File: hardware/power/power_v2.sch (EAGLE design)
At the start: 43 parts, among them J1 FASTON1289_ST, J2 FASTON1289_ST, J3 12v, J4 5v, J5 XT30PW-F, J6 XT30PW-F, J7 XT30PW-F, J8 XT30PW-F, Q1 MMBT5401L, Q2 PSMN1R0-40YSH, U1 PDQ30-Q24-S5-D, U2 PDQ30-Q24-S12-D

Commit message: Going to rework power plane v2
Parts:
- added C11: 0.01uF, timlib:C_CERAMIC_1210
- added C12: 2.2n, timlib:C_CERAMIC_1210
- added C13: 16nF, timlib:C_CERAMIC_1210
- added D3: SMAJ30A, timlib:SMAJ30A
- added D4: SK510A-LTP, timlib:SK510A-LTP
- added Q3: MMBT5401L, timlib:MMBT5401L
- added Q4: PSMN1R0-40YSH, timlib:PSMN1R0-40YSH
- added R10: 18.9k, rcl:R-US_R0603
- added R11: 18.9, rcl:R-US_R0603
- added R12: PMR25HZPFV, timlib:PMR25HZPFV
- added R7: 47.5k, rcl:R-US_R0603
- added R8: 3.4k, rcl:R-US_R0603
- added R9: 4.32k, rcl:R-US_R0603
- added U$13: 2-PIN, timlib:2-PIN
- added U$14: LM5069_DGS_10, timlib:LM5069_DGS_10
- added U$22: 1N4148W-7-F, timlib:1N4148W-7-F
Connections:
- removed net ISO_GND: U1.-VIN, U2.-VIN
- new net MOSFET_DRAIN1: Q4.D, R12.2
- new net N$12: R8.2, R9.1, U$14.OVLO
- new net N$13: R7.1, U$13.P$2
- new net N$14: Q4.G, R11.1, U$14.GATE, U$22.A
- new net N$15: R10.1, U$14.PWR
- new net N$16: C12.1, U$14.TIMER
- new net N$17: C13.1, Q3.E, U$22.C
- new net N$18: Q3.B, R11.2
- new net N$19: R12.1K, U$14.VIN
- new net N$20: R12.2K, U$14.SEN
- new net N$4: R7.2, R8.1, U$14.UVLO
- net +24V_BATT: now also C11.1, D3.C, R12.1, U$13.P$1; no longer U1.+VIN, U2.+VIN
- net +24V_ISO: now also D4.C, Q4.S, U$14.OUT, U1.+VIN, U2.+VIN
- net GND_BATT: now also C11.2, C12.2, C13.2, D3.A, D4.A, Q3.C, R10.2, R9.2, U$14.GND, U1.-VIN, U2.-VIN

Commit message: Happy with this layout
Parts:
- removed C11: 0.01uF, timlib:C_CERAMIC_1210
- removed U$6: 1N4148W-7-F, timlib:1N4148W-7-F
- D3: value SMAJ30A -> 1N4148W-7-F; device timlib:SMAJ30A -> timlib:1N4148W-7-F
- renumbered U$22 to D5
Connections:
- net +24V_BATT: no longer C11.1, D3.C
- net GND_BATT: no longer C11.2, D3.A
- net N$5: now also D3.A; no longer U$6.A
- net N$8: now also D3.C; no longer U$6.C

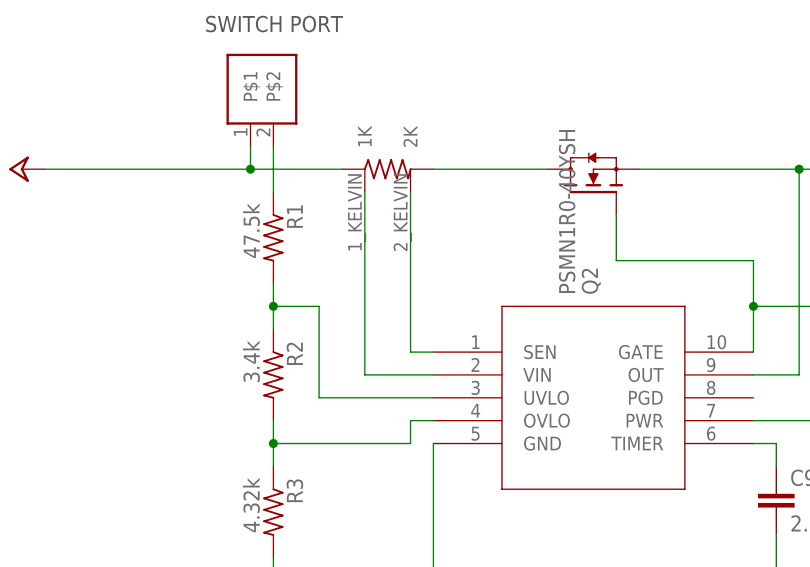
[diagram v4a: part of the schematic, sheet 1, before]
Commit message: Added more accurate current limit resistors
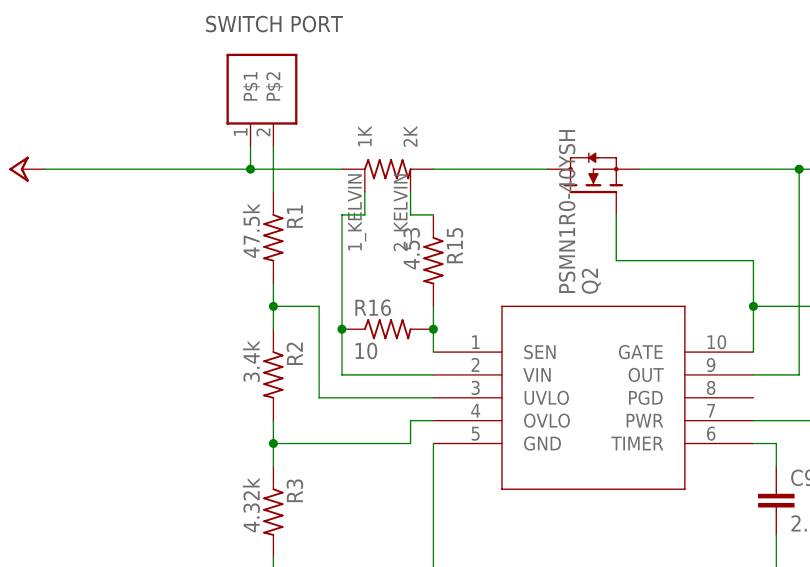
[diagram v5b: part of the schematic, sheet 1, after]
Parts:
- added R13, R16: 10, rcl:R-US_R0603
- added R14, R15: 4.53, rcl:R-US_R0603
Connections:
- new net N$21: R12.2K, R14.1
- new net N$22: R12.1K, R13.2, U$14.VIN
- net N$10: now also R15.2, R16.2, U$1.SEN; no longer R4.1K, U$1.VIN
- net N$11: now also R15.1; no longer U$1.SEN
- net N$19: now also R16.1, R4.1K, U$1.VIN; no longer R12.1K, U$14.VIN
- net N$20: now also R13.1, R14.2; no longer R12.2K
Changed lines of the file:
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@@
 <part name="D3" library="timlib" library_urn="urn:adsk.eagle:library:16152524" deviceset="1N4148W-7-F" device="" package3d_urn="urn:adsk.eagle:package:16502213/2"/>
 <part name="D5" library="timlib" library_urn="urn:adsk.eagle:library:16152524" deviceset="1N4148W-7-F" device="" package3d_urn="urn:adsk.eagle:package:16502213/2"/>
+<part name="R13" library="rcl" library_urn="urn:adsk.eagle:library:334" deviceset="R-US_" device="R0603" package3d_urn="urn:adsk.eagle:package:23555/3" value="10"/>
+<part name="R14" library="rcl" library_urn="urn:adsk.eagle:library:334" deviceset="R-US_" device="R0603" package3d_urn="urn:adsk.eagle:package:23555/3" value="4.53"/>
+<part name="R15" library="rcl" library_urn="urn:adsk.eagle:library:334" deviceset="R-US_" device="R0603" package3d_urn="urn:adsk.eagle:package:23555/3" value="4.53"/>
+<part name="R16" library="rcl" library_urn="urn:adsk.eagle:library:334" deviceset="R-US_" device="R0603" package3d_urn="urn:adsk.eagle:package:23555/3" value="10"/>
 </parts>
 <sheets>
@@
 <attribute name="NAME" x="180.34" y="106.68" size="1.778" layer="95"/>
 <attribute name="VALUE" x="180.34" y="100.33" size="1.778" layer="96"/>
+</instance>
+<instance part="R15" gate="G$1" x="119.38" y="114.3" smashed="yes" rot="R270">
+<attribute name="NAME" x="120.8786" y="118.11" size="1.778" layer="95" rot="R270"/>
+<attribute name="VALUE" x="116.078" y="118.11" size="1.778" layer="96" rot="R270"/>
+</instance>
+<instance part="R16" gate="G$1" x="114.3" y="106.68" smashed="yes">
+<attribute name="NAME" x="110.49" y="108.1786" size="1.778" layer="95"/>
+<attribute name="VALUE" x="110.49" y="103.378" size="1.778" layer="96"/>
 </instance>
 </instances>
@@
 <net name="N$10" class="0">
 <segment>
+<pinref part="U$1" gate="A" pin="SEN"/>
+<pinref part="R16" gate="G$1" pin="2"/>
+<wire x1="119.38" y1="104.14" x2="119.38" y2="106.68" width="0.1524" layer="91"/>
+<pinref part="R15" gate="G$1" pin="2"/>
+<wire x1="119.38" y1="106.68" x2="119.38" y2="109.22" width="0.1524" layer="91"/>
+<junction x="119.38" y="106.68"/>
+</segment>
+</net>
+<net name="N$11" class="0">
+<segment>
+<pinref part="R15" gate="G$1" pin="1"/>
+<pinref part="R4" gate="A" pin="2K"/>
+<wire x1="119.38" y1="119.38" x2="116.84" y2="119.38" width="0.1524" layer="91"/>
+<wire x1="116.84" y1="119.38" x2="116.84" y2="121.92" width="0.1524" layer="91"/>
+</segment>
+</net>
+<net name="N$19" class="0">
+<segment>
+<pinref part="R4" gate="A" pin="1K"/>
+<wire x1="111.76" y1="121.92" x2="111.76" y2="119.38" width="0.1524" layer="91"/>
+<wire x1="111.76" y1="119.38" x2="109.22" y2="119.38" width="0.1524" layer="91"/>
+<pinref part="R16" gate="G$1" pin="1"/>
+<wire x1="109.22" y1="119.38" x2="109.22" y2="106.68" width="0.1524" layer="91"/>
 <pinref part="U$1" gate="A" pin="VIN"/>
-<wire x1="119.38" y1="101.6" x2="111.76" y2="101.6" width="0.1524" layer="91" grouprefs="LEG_SOFTSTART"/>
-<pinref part="R4" gate="A" pin="1K"/>
-<wire x1="111.76" y1="121.92" x2="111.76" y2="101.6" width="0.1524" layer="91" grouprefs="LEG_SOFTSTART"/>
-</segment>
-</net>
-<net name="N$11" class="0">
-<segment>
-<pinref part="R4" gate="A" pin="2K"/>
-<wire x1="116.84" y1="121.92" x2="116.84" y2="104.14" width="0.1524" layer="91" grouprefs="LEG_SOFTSTART"/>
-<pinref part="U$1" gate="A" pin="SEN"/>
-<wire x1="116.84" y1="104.14" x2="119.38" y2="104.14" width="0.1524" layer="91" grouprefs="LEG_SOFTSTART"/>
+<wire x1="109.22" y1="106.68" x2="109.22" y2="101.6" width="0.1524" layer="91"/>
+<wire x1="109.22" y1="101.6" x2="119.38" y2="101.6" width="0.1524" layer="91"/>
+<junction x="109.22" y="106.68"/>
 </segment>
 </net>
@@
 <attribute name="NAME" x="142.24" y="96.52" size="1.778" layer="95"/>
 <attribute name="VALUE" x="142.24" y="90.17" size="1.778" layer="96"/>
+</instance>
+<instance part="R13" gate="G$1" x="76.2" y="96.52" smashed="yes" rot="R180">
+<attribute name="NAME" x="80.01" y="95.0214" size="1.778" layer="95" rot="R180"/>
+<attribute name="VALUE" x="80.01" y="99.822" size="1.778" layer="96" rot="R180"/>
+</instance>
+<instance part="R14" gate="G$1" x="81.28" y="104.14" smashed="yes" rot="R270">
+<attribute name="NAME" x="82.7786" y="107.95" size="1.778" layer="95" rot="R270"/>
+<attribute name="VALUE" x="77.978" y="107.95" size="1.778" layer="96" rot="R270"/>
 </instance>
 </instances>
@@
 </segment>
 </net>
-<net name="N$19" class="0">
-<segment>
-<wire x1="81.28" y1="91.44" x2="73.66" y2="91.44" width="0.1524" layer="91" grouprefs="ISO_SOFTSTART"/>
-<wire x1="73.66" y1="111.76" x2="73.66" y2="91.44" width="0.1524" layer="91" grouprefs="ISO_SOFTSTART"/>
+<net name="N$20" class="0">
+<segment>
+<wire x1="81.28" y1="96.52" x2="81.28" y2="93.98" width="0.1524" layer="91" grouprefs="ISO_SOFTSTART"/>
+<pinref part="U$14" gate="A" pin="SEN"/>
+<pinref part="R13" gate="G$1" pin="1"/>
+<pinref part="R14" gate="G$1" pin="2"/>
+<wire x1="81.28" y1="96.52" x2="81.28" y2="99.06" width="0.1524" layer="91"/>
+<junction x="81.28" y="96.52"/>
+</segment>
+</net>
+<net name="N$21" class="0">
+<segment>
+<pinref part="R14" gate="G$1" pin="1"/>
+<pinref part="R12" gate="A" pin="2K"/>
+<wire x1="81.28" y1="109.22" x2="78.74" y2="109.22" width="0.1524" layer="91"/>
+<wire x1="78.74" y1="109.22" x2="78.74" y2="111.76" width="0.1524" layer="91"/>
+</segment>
+</net>
+<net name="N$22" class="0">
+<segment>
+<pinref part="R12" gate="A" pin="1K"/>
+<wire x1="73.66" y1="111.76" x2="73.66" y2="109.22" width="0.1524" layer="91"/>
+<wire x1="73.66" y1="109.22" x2="71.12" y2="109.22" width="0.1524" layer="91"/>
+<pinref part="R13" gate="G$1" pin="2"/>
+<wire x1="71.12" y1="109.22" x2="71.12" y2="96.52" width="0.1524" layer="91"/>
+<wire x1="81.28" y1="91.44" x2="71.12" y2="91.44" width="0.1524" layer="91" grouprefs="ISO_SOFTSTART"/>
 <pinref part="U$14" gate="A" pin="VIN"/>
-<pinref part="R12" gate="A" pin="1K"/>
-</segment>
-</net>
-<net name="N$20" class="0">
-<segment>
-<wire x1="78.74" y1="111.76" x2="78.74" y2="93.98" width="0.1524" layer="91" grouprefs="ISO_SOFTSTART"/>
-<wire x1="78.74" y1="93.98" x2="81.28" y2="93.98" width="0.1524" layer="91" grouprefs="ISO_SOFTSTART"/>
-<pinref part="U$14" gate="A" pin="SEN"/>
-<pinref part="R12" gate="A" pin="2K"/>
-</segment>
-</net>
+<wire x1="71.12" y1="96.52" x2="71.12" y2="91.44" width="0.1524" layer="91"/>
+<junction x="71.12" y="96.52"/>
+</segment>
+</net>

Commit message: Reordered schematic
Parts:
- R12, R4: value PMR25HZPFV -> PMR25HZPFV1L00; device timlib:PMR25HZPFV -> timlib:PMR25HZPFV1L00
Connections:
- net +24V_LEG renamed +24V_POWER
- net MOSFET_DRAIN: now also R12.2; no longer R4.2
- net MOSFET_DRAIN1: now also R4.2; no longer R12.2
- net N$11: now also R12.2K; no longer R4.2K
- net N$19: now also R12.1K; no longer R4.1K
- net N$21: now also R4.2K; no longer R12.2K
- net N$22: now also R4.1K; no longer R12.1K

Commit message: Updates to power board
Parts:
- removed C23: 10uF, timlib:C_CERAMIC_1210
- removed U$13, U$26: 2-PIN, timlib:2-PIN
- added C11: 2.2nF, rcl:C-EUC0603
- added H1, H2, H3, H4, H5, H6: GND_HOLE_M3, timlib:GND_HOLE_M3
- added J100, J101: FASTON1289_ST, timlib:FASTON1289_ST
- C1, C2, C3, C4, C5, C6, C7: value 220uf -> 10uF; device timlib:35ZLH220MEFC8X11.5 -> timlib:C_CERAMIC_1210
- C10: value 16nF -> 10uF
- C12: value 2.2n -> 0.01uF
- C13: value 16nF -> 47nF; device timlib:C_CERAMIC_1210 -> rcl:C-EUC0603
- C14: value 10uF -> 2.2nF; device timlib:C_CERAMIC_1210 -> rcl:C-EUC0603
- C15, C17, C18, C19, C20, C21, C22: value 10uF -> 220uf; device timlib:C_CERAMIC_1210 -> timlib:35ZLH220MEFC8X11.5
- C16: value 10uF -> 47nF; device timlib:C_CERAMIC_1210 -> rcl:C-EUC0603
- C8: value 0.01uF -> 2.2nF
- C9: value 2.2n -> 10uF
- D1: value SMAJ30A -> SK510A-LTP; device timlib:SMAJ30A -> timlib:SK510A-LTP
- D2: value SK510A-LTP -> SMAJ30A; device timlib:SK510A-LTP -> timlib:SMAJ30A
- D4: value SK510A-LTP -> 1N4148W-7-F; device timlib:SK510A-LTP -> timlib:1N4148W-7-F
- D5: value 1N4148W-7-F -> SK510A-LTP; device timlib:1N4148W-7-F -> timlib:SK510A-LTP
- J1: value FASTON1289_ST -> 12v; device timlib:FASTON1289_ST -> timlib:MOLEX_4_RA
- J2: value FASTON1289_ST -> 5v; device timlib:FASTON1289_ST -> timlib:MOLEX_4_RA
- J3: value 12v -> XT30PW-F; device timlib:MOLEX_4_RA -> timlib:XT30PW-F
- J4: value 5v -> XT30PW-F; device timlib:MOLEX_4_RA -> timlib:XT30PW-F
- J7, J8: value XT30PW-F -> 2-PIN; device timlib:XT30PW-F -> timlib:2-PIN
- Q1: value MMBT5401L -> PSMN1R0-40YSH; device timlib:MMBT5401L -> timlib:PSMN1R0-40YSH
- Q2: value PSMN1R0-40YSH -> MMBT5401L; device timlib:PSMN1R0-40YSH -> timlib:MMBT5401L
- R1: value 47.5k -> 4.32k
- R10: value 18.9k -> 3.4k
- R11: value 18.9 -> 1k
- R12: value PMR25HZPFV1L00 -> 18.9k; device timlib:PMR25HZPFV1L00 -> rcl:R-US_R0603
- R13: value 10 -> 18.9k
- R15: value 4.53 -> 4.32k
- R16: value 10 -> 1k
- R3, R9: value 4.32k -> 47.5k
- R4: value PMR25HZPFV1L00 -> 4.53; device timlib:PMR25HZPFV1L00 -> rcl:R-US_R0603
- R5: value 18.9k -> 10
- R6: value 18.9 -> 10
- R7: value 47.5k -> 0.002; device rcl:R-US_R0603 -> timlib:PMR25HZPFV2L00
- R8: value 3.4k -> 0.002; device rcl:R-US_R0603 -> timlib:PMR25HZPFV2L00
- U1: value PDQ30-Q24-S5-D -> PDQ30-Q24-S12-D; device timlib:PDQ30-Q24-S5-D -> timlib:PDQ30-Q24-S12-D
- U2: value PDQ30-Q24-S12-D -> PDQ30-Q24-S5-D; device timlib:PDQ30-Q24-S12-D -> timlib:PDQ30-Q24-S5-D
- renumbered U$1 to U3, U$14 to U4
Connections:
- net +12VOUT: now also J1.CONN2, J1.CONN4, U1.+12VOUT; no longer J3.CONN2, J3.CONN4, U2.+12VOUT
- net +24V_BATT: now also C12.1, D2.C, J101.PIN1, J7.P$1, J8.P$1, R7.1, R8.1; no longer C8.1, D1.C, J1.PIN1, R12.1, R4.1, U$13.P$1, U$26.P$1
- net +24V_ISO: now also C1.1, C10.1, C2.1, C3.1, C4.1, C5.1, C6.1, C7.1, C8.1, C9.1, D1.C, Q1.S; no longer C14.1, C15.1, C16.1, C17.1, C18.1, C19.1, C20.1, C21.1, C22.1, C23.1, D4.C, Q4.S
- net +24V_POWER: now also C15.+, C17.+, C18.+, C19.+, C20.+, C21.+, C22.+, D5.C, J3.V+, J4.V+, Q4.S; no longer C1.+, C2.+, C3.+, C4.+, C5.+, C6.+, C7.+, D2.C, J7.V+, J8.V+, Q2.S
- net +5VOUT: now also J2.CONN2, J2.CONN4, U2.+5VOUT; no longer J4.CONN2, J4.CONN4, U1.+5VOUT
- net 12V_GND: now also J1.CONN1, J1.CONN3, U1.12V_GND; no longer J3.CONN1, J3.CONN3, U2.12V_GND
- net 5V_GND: now also J2.CONN1, J2.CONN3, U2.5V_GND; no longer J4.CONN1, J4.CONN3, U1.5V_GND
- net GND_BATT: now also C1.2, C11.2, C15.-, C17.-, C18.-, C19.-, C2.2, C20.-, C21.-, C22.-, C3.2, C4.2, C5.2, C6.2, C7.2, D5.A, H1.GND_HOLE, H2.GND_HOLE, H3.GND_HOLE, H4.GND_HOLE, H5.GND_HOLE, H6.GND_HOLE, J100.PIN1, J3.V-, J4.V-, Q2.C, R1.2, R12.2, R13.2, R15.2; no longer C1.-, C15.2, C17.2, C18.2, C19.2, C2.-, C20.2, C21.2, C22.2, C23.2, C3.-, C4.-, C5.-, C6.-, C7.-, D4.A, J2.PIN1, J7.V-, J8.V-, Q1.C, R10.2, R3.2, R5.2, R9.2
- net MOSFET_DRAIN: now also Q4.D, R8.2; no longer Q2.D, R12.2
- net MOSFET_DRAIN1: now also Q1.D, R7.2; no longer Q4.D, R4.2
- net N$1: now also R10.1, R9.2; no longer R1.2, R2.1
- net N$10: now also R14.2, R6.2; no longer R15.2, R16.2
- net N$11: now also R14.1, R8.2K; no longer R12.2K, R15.1
- net N$12: now also R1.1, R2.2; no longer R8.2, R9.1
- net N$13: now also J7.P$2, R3.1; no longer R7.1, U$13.P$2
- net N$14: now also D3.A, Q1.G; no longer D5.A, Q4.G
- net N$15: now also R12.1; no longer R10.1
- net N$16: now also C11.1; no longer C12.1
- net N$17: now also D3.C, Q2.E; no longer D5.C, Q3.E
- net N$18: now also Q2.B; no longer Q3.B
- net N$19: now also R6.1, R8.1K; no longer R12.1K, R16.1
- net N$2: now also R10.2, R15.1; no longer R2.2, R3.1
- net N$20: now also R4.2, R5.1; no longer R13.1, R14.2
- net N$21: now also R4.1, R7.2K; no longer R14.1, R4.2K
- net N$22: now also R5.2, R7.1K; no longer R13.2, R4.1K
- net N$3: now also J8.P$2, R9.1; no longer R1.1, U$26.P$2
- net N$4: now also R2.1, R3.2; no longer R7.2, R8.1
- net N$5: now also D4.A, Q4.G, R16.1; no longer D3.A, Q2.G, R6.1
- net N$6: now also R13.1; no longer R5.1
- net N$7: now also C14.1; no longer C9.1
- net N$8: now also C16.1, D4.C, Q3.E; no longer C10.1, D3.C, Q1.E
- net N$9: now also Q3.B, R16.2; no longer Q1.B, R6.2
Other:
- moved on the sheet: J5, J6, R10, R15, R16, R6
